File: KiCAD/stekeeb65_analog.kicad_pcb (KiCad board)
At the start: 2 copper layers, 3.4 x 3 mm, 349 parts, among them IC1 ADS7953SBDBTR, IC2 ADS7953SBDBTR, IC3 ADS7953SBDBTR, IC4 ADS7953SBDBTR, IC5 IS31FL3733B-TQLS4, IC6 IS31FL3733B-TQLS4, J1 Conn_01x04, J2 Conn_01x03, SW1 MX_Lekker, SW10 MX_Lekker, SW11 MX_Lekker, SW12 MX_Lekker, SW13 MX_Lekker, SW14 MX_Lekker, SW15 MX_Lekker, SW16 MX_Lekker, SW17 MX_Lekker, SW18 MX_Lekker, SW19 MX_Lekker, SW2 MX_Lekker, SW20 MX_Lekker, SW21 MX_Lekker, SW22 MX_Lekker, SW23 MX_Lekker, SW24 MX_Lekker, SW25 MX_Lekker, SW26 MX_Lekker, SW27 MX_Lekker, SW28 MX_Lekker, SW29 MX_Lekker, SW3 MX_Lekker, SW30 MX_Lekker, SW31 MX_Lekker, SW32 MX_Lekker, SW33 MX_Lekker, SW34 MX_Lekker, SW35 MX_Lekker, SW36 MX_Lekker, SW37 MX_Lekker, SW38 MX_Lekker, SW39 MX_Lekker, SW4 MX_Lekker, SW40 MX_Lekker, SW41 MX_Lekker, SW42 MX_Lekker, SW43 MX_Lekker, SW44 MX_Lekker, SW45 MX_Lekker, SW46 MX_Lekker, SW47 MX_Lekker, SW48 MX_Lekker, SW49 MX_Lekker, SW5 MX_Lekker, SW50 MX_Lekker, SW51 MX_Lekker, SW52 MX_Lekker, SW53 MX_Lekker, SW54 MX_Lekker, SW55 MX_Lekker, SW56 MX_Lekker, SW57 MX_Lekker, SW58 MX_Lekker, SW59 MX_Lekker, SW6 MX_Lekker, SW60 MX_Lekker, SW61 MX_Lekker, SW62 MX_Lekker, SW63 MX_Lekker, SW64 MX_Lekker, SW65 MX_Lekker, SW66 MX_Lekker, SW67 MX_Lekker, SW68 MX_Lekker, SW7 MX_Lekker, SW8 MX_Lekker, SW9 MX_Lekker, U1 AH49-E, U10 AH49-E, U11 AH49-E, U12 AH49-E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

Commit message: Apply script to layout
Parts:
- moved S1 367.6 mm to (9.53, 4.03)
- moved S16 361.9 mm to (14.3, 23.1)
- moved S3 347.8 mm to (47.6, 4.03)
- moved C1 336.5 mm to (12.3, 10.0)
- moved U1 327.8 mm to (9.53, 9.53)
- moved S59 319.4 mm to (11.9, 80.2)
- moved S32 317.4 mm to (42.9, 42.1)
- moved S4 317.3 mm to (66.7, 4.03)
- moved C16 315.3 mm to (17.0, 29.1)
- moved S2 314.7 mm to (28.6, 4.03)
- moved U3 314.0 mm to (47.6, 9.53)
- moved C2 310.9 mm to (31.3, 10.0)
- moved C31 306.8 mm to (19.4, 48.1)
- moved S31 306.7 mm to (16.7, 42.1)
- moved U16 300.5 mm to (14.3, 28.6)
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
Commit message: Update Lekker footprints to include non-1U sizes and stabilizers
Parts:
- SW14: footprint MX_Only:MX_Lekker -> MX_Only:MX_Lekker-2U
- SW16, SW29: footprint MX_Only:MX_Lekker -> MX_Only:MX_Lekker-1.5U
- SW31: footprint MX_Only:MX_Lekker -> MX_Only:MX_Lekker-1.75U
- SW43, SW45: footprint MX_Only:MX_Lekker -> MX_Only:MX_Lekker-2.25U
- SW59, SW60, SW61: footprint MX_Only:MX_Lekker -> MX_Only:MX_Lekker-1.25U
- SW62: footprint MX_Only:MX_Lekker -> MX_Only:MX_Lekker-6.25U-ReversedStabilizers
- moved IC5 44.3 mm to (140.0, 253.0)
- moved IC6 36.7 mm to (159.9, 253.3)
- moved IC3 5.08 mm to (22.4, 233.1)

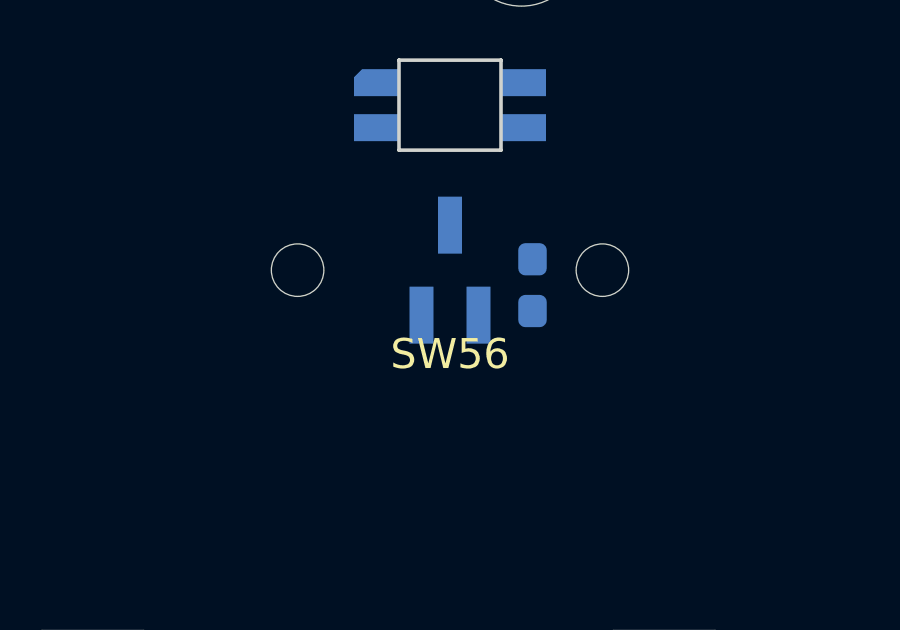
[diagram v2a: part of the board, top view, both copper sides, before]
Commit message: Fix right shift not having the 1.75U footprint
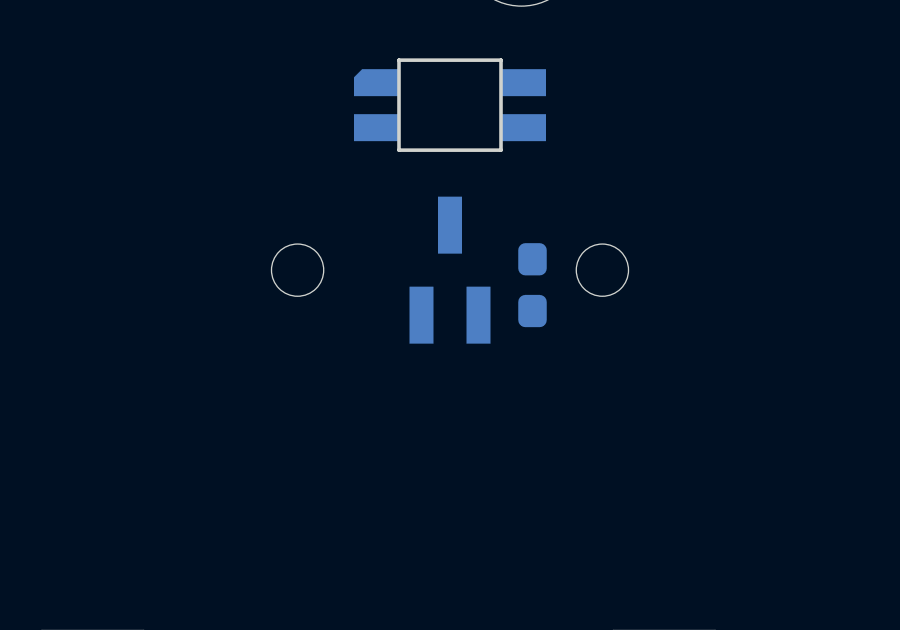
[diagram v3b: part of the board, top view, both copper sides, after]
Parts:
- SW56: footprint MX_Only:MX_Lekker -> MX_Only:MX_Lekker-1.75U
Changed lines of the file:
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@@
     (pad "" np_thru_hole circle (at 5.08 0 48.0996) (size 1.75 1.75) (drill 1.75) (layers *.Cu *.Mask))
   )
-  (footprint "MX_Only:MX_Lekker" (layer "F.Cu")
+  (footprint "MX_Only:MX_Lekker-1.75U" (layer "F.Cu")
     (at 250.0312 66.675)
     (property "Sheetfile" "keys.kicad_sch")
     (property "Sheetname" "Keys")
-    (fp_text reference "SW56" (at 0 2.8 unlocked) (layer "F.SilkS")
+    (attr through_hole)
+    (fp_text reference "SW56" (at 0 3.175) (layer "Dwgs.User")
       (effects (font (size 1 1) (thickness 0.15)))
     )
-    (fp_text value "MX_Lekker" (at 0 2.8 unlocked) (layer "F.Fab") hide
+    (fp_text value "MX_Lekker" (at 0 -7.9375) (layer "Dwgs.User")
       (effects (font (size 1 1) (thickness 0.15)))
     )
-    (fp_text user "${REFERENCE}" (at 0 4.2 unlocked) (layer "F.Fab")
-      (effects (font (size 1 1) (thickness 0.15)))
-    )
+    (fp_line (start 5 -7) (end 7 -7) (layer "Dwgs.User") (width 0.15))
     (fp_line (start -7 -7) (end -7 -5) (layer "Dwgs.User") (width 0.15))
-    (fp_line (start -9.525 9.525) (end -9.525 -9.525) (layer "Dwgs.User") (width 0.15))
-    (fp_line (start -9.525 -9.525) (end 9.525 -9.525) (layer "Dwgs.User") (width 0.15))
+    (fp_line (start -16.66875 9.525) (end 16.66875 9.525) (layer "Dwgs.User") (width 0.15))
+    (fp_line (start 16.66875 -9.525) (end 16.66875 9.525) (layer "Dwgs.User") (width 0.15))
+    (fp_line (start -16.66875 -9.525) (end 16.66875 -9.525) (layer "Dwgs.User") (width 0.15))
+    (fp_line (start -7 7) (end -5 7) (layer "Dwgs.User") (width 0.15))
+    (fp_line (start -16.66875 9.525) (end -16.66875 -9.525) (layer "Dwgs.User") (width 0.15))
+    (fp_line (start 7 7) (end 7 5) (layer "Dwgs.User") (width 0.15))
     (fp_line (start 5 7) (end 7 7) (layer "Dwgs.User") (width 0.15))
+    (fp_line (start 7 -7) (end 7 -5) (layer "Dwgs.User") (width 0.15))
+    (fp_line (start -7 5) (end -7 7) (layer "Dwgs.User") (width 0.15))
     (fp_line (start -5 -7) (end -7 -7) (layer "Dwgs.User") (width 0.15))
-    (fp_line (start -7 7) (end -5 7) (layer "Dwgs.User") (width 0.15))
-    (fp_line (start 7 7) (end 7 5) (layer "Dwgs.User") (width 0.15))
-    (fp_line (start -7 5) (end -7 7) (layer "Dwgs.User") (width 0.15))
-    (fp_line (start 7 -7) (end 7 -5) (layer "Dwgs.User") (width 0.15))
-    (fp_line (start 9.525 9.525) (end -9.525 9.525) (layer "Dwgs.User") (width 0.15))
-    (fp_line (start 9.525 -9.525) (end 9.525 9.525) (layer "Dwgs.User") (width 0.15))
-    (fp_line (start 5 -7) (end 7 -7) (layer "Dwgs.User") (width 0.15))
-    (pad "" np_thru_hole circle (at -5.08 0 48.0996) (size 1.75 1.75) (drill 1.75) (layers *.Cu *.Mask))
-    (pad "" np_thru_hole circle (at 5.08 0 48.0996) (size 1.75 1.75) (drill 1.75) (layers *.Cu *.Mask))
+    (pad "" np_thru_hole circle (at -5.08 0 48.099) (size 1.74 1.74) (drill 1.74) (layers F&B.Cu *.Mask))
+    (pad "" np_thru_hole circle (at 5.08 0 48.099) (size 1.74 1.74) (drill 1.74) (layers F&B.Cu *.Mask))
   )
   (footprint "MX_Only:MX_Lekker" (layer "F.Cu")

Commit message: Committing before changing to MUX design
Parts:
- added SW69: RotaryEncoder_Switch, mini-general-tweaks:RotaryEncoder_Alps_EC11E-Switch-Vertical-EDIT, F.Cu at (245.0, 133.6)
- moved IC2 292.3 mm to (228.6, 16.3), turned to -90 degrees
- moved IC1 212.7 mm to (66.7, 35.5), turned to -90 degrees
- moved IC4 192.8 mm to (109.6, 54.4), turned to -90 degrees
- moved J1 29.0 mm to (91.2, 233.0)
- moved IC3 13.9 mm to (22.5, 247.0)
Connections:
- IC1 pad 11: SW_6 -> SW_31
- IC1 pad 12: SW_5 -> SW_16
- IC1 pad 13: SW_4 -> SW_1
- IC1 pad 14: SW_3 -> SW_2
- IC1 pad 15: SW_2 -> SW_3
- IC1 pad 16: SW_1 -> SW_4
- IC1 pad 17: SW_16 -> SW_5
- IC1 pad 18: SW_31 -> SW_6
- IC2 pad 11: unconnected-(IC2-Pad11) -> SW_7
- IC2 pad 12: unconnected-(IC2-Pad12) -> SW_8
- IC2 pad 13: unconnected-(IC2-Pad13) -> SW_9
- IC2 pad 14: unconnected-(IC2-Pad14) -> SW_10
- IC2 pad 15: unconnected-(IC2-Pad15) -> SW_11
- IC2 pad 16: unconnected-(IC2-Pad16) -> SW_12
- IC2 pad 17: unconnected-(IC2-Pad17) -> SW_13
- IC2 pad 18: unconnected-(IC2-Pad18) -> SW_14
- IC2 pad 21: unconnected-(IC2-Pad21) -> SW_29
- IC2 pad 22: unconnected-(IC2-Pad22) -> SW_28
- IC2 pad 23: unconnected-(IC2-Pad23) -> SW_27
- IC2 pad 24: unconnected-(IC2-Pad24) -> SW_26
- IC2 pad 25: unconnected-(IC2-Pad25) -> SW_25
- IC2 pad 26: unconnected-(IC2-Pad26) -> SW_24
- IC2 pad 27: unconnected-(IC2-Pad27) -> SW_23
- IC2 pad 28: unconnected-(IC2-Pad28) -> SW_22
- IC2 pad 31: unconnected-(IC2-Pad31) -> SPI1_CS
- IC2 pad 32: unconnected-(IC2-Pad32) -> SPI1_SCLK
- IC2 pad 33: unconnected-(IC2-Pad33) -> SPI1_MOSI
- IC2 pad 34: unconnected-(IC2-Pad34) -> SPI1_MISO
- IC3 pad 31: unconnected-(IC3-Pad31) -> SPI1_CS
- IC3 pad 32: unconnected-(IC3-Pad32) -> SPI1_SCLK
- IC3 pad 33: unconnected-(IC3-Pad33) -> SPI1_MOSI
- IC3 pad 34: unconnected-(IC3-Pad34) -> SPI1_MISO
- IC4 pad 11: unconnected-(IC4-Pad11) -> SW_45
- IC4 pad 12: unconnected-(IC4-Pad12) -> SW_46
- IC4 pad 13: unconnected-(IC4-Pad13) -> SW_47
- IC4 pad 14: unconnected-(IC4-Pad14) -> SW_48
- IC4 pad 15: unconnected-(IC4-Pad15) -> SW_35
- IC4 pad 16: unconnected-(IC4-Pad16) -> SW_36
- IC4 pad 17: unconnected-(IC4-Pad17) -> SW_37
- IC4 pad 18: unconnected-(IC4-Pad18) -> SW_38
- IC4 pad 21: unconnected-(IC4-Pad21) -> SW_52
- IC4 pad 22: unconnected-(IC4-Pad22) -> SW_51
- IC4 pad 23: unconnected-(IC4-Pad23) -> SW_50
- IC4 pad 24: unconnected-(IC4-Pad24) -> SW_49
- IC4 pad 25: unconnected-(IC4-Pad25) -> SW_62
- IC4 pad 26: unconnected-(IC4-Pad26) -> SW_61
- IC4 pad 27: unconnected-(IC4-Pad27) -> SW_60
- IC4 pad 28: unconnected-(IC4-Pad28) -> SW_59
- IC4 pad 31: unconnected-(IC4-Pad31) -> SPI0_CS
- IC4 pad 32: unconnected-(IC4-Pad32) -> SPI0_SCLK
- IC4 pad 33: unconnected-(IC4-Pad33) -> SPI0_MOSI
- IC4 pad 34: unconnected-(IC4-Pad34) -> SPI0_MISO
- U70 pad 38: SW_15 -> unconnected-(U70-Pad38)
- U70 pad 39: SW_30 -> unconnected-(U70-Pad39)
- U70 pad 40: SW_44 -> unconnected-(U70-Pad40)
- U70 pad 41: SW_58 -> unconnected-(U70-Pad41)
